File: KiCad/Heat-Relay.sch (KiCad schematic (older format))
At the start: 6 parts, among them K1 G5LE-1A-E_DC12, Q2 MJE340

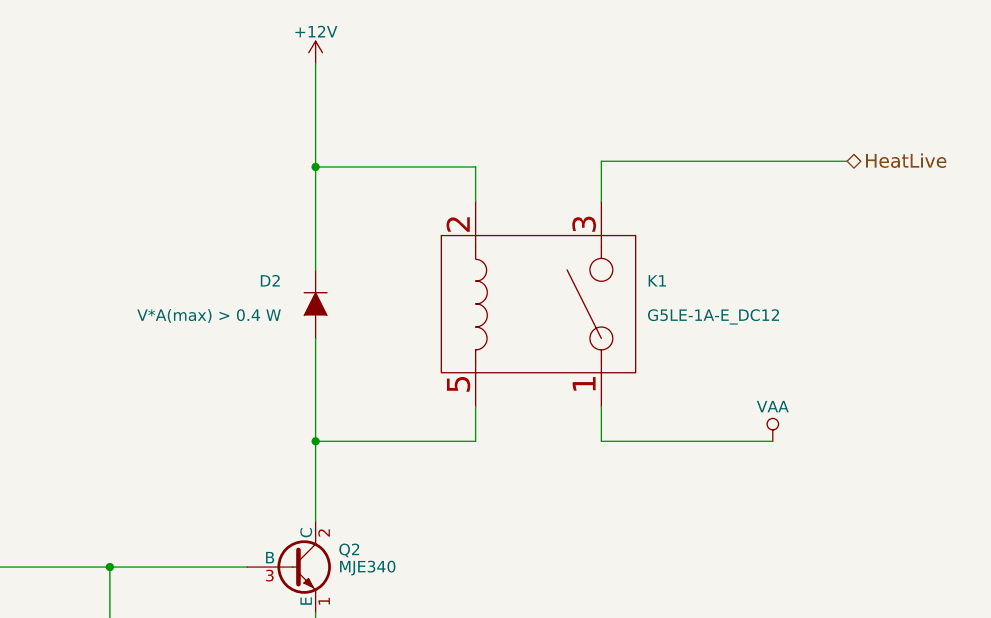
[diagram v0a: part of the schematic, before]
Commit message: power supply placed and routed
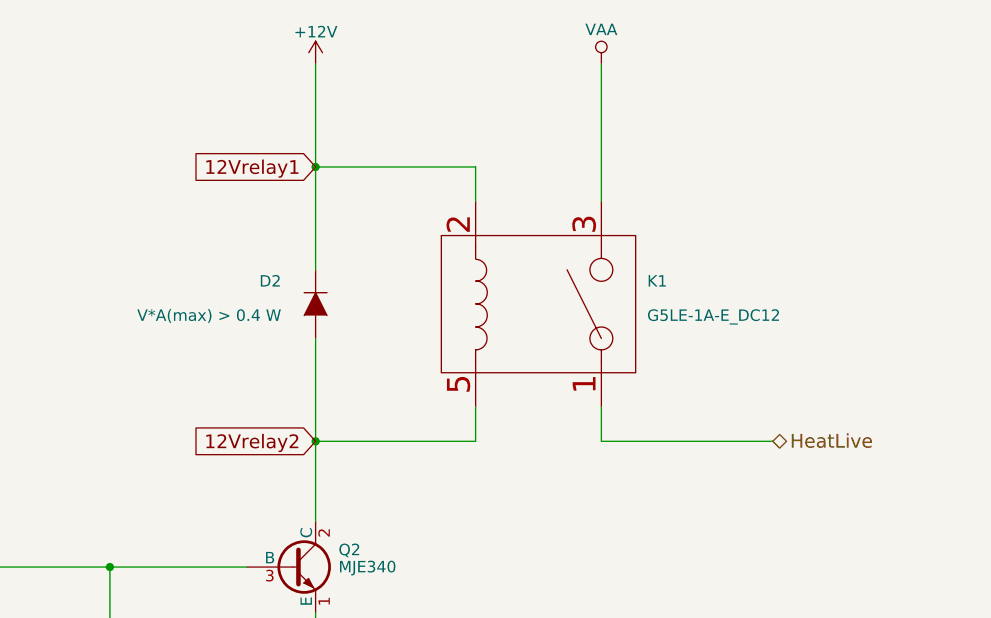
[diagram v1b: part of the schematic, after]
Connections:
- net HeatLive: now also K1.1 (contact_1); no longer K1.3 (contact_2)
- net VAA: now also K1.3 (contact_2); no longer K1.1 (contact_1)
- net 12Vrelay2: now reaches D2.2 (A), K1.5 (coil_2), Q2.2 (C)
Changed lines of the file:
@@
 	0    1    1    0
 $EndComp
-Text HLabel 8725 2625 2    60   BiDi ~ 0
+Text HLabel 8400 3850 2    60   BiDi ~ 0
 HeatLive
 $Comp
 L VAA #PWR024
 U 1 1 56800D0A
-P 8400 3850
-F 0 "#PWR024" H 8400 3700 50  0001 C CNN
-F 1 "VAA" H 8400 4000 50  0000 C CNN
-F 2 "" H 8400 3850 50  0000 C CNN
-F 3 "" H 8400 3850 50  0000 C CNN
-	1    8400 3850
+P 7650 2200
+F 0 "#PWR024" H 7650 2050 50  0001 C CNN
+F 1 "VAA" H 7650 2350 50  0000 C CNN
+F 2 "" H 7650 2200 50  0000 C CNN
+F 3 "" H 7650 2200 50  0000 C CNN
+	1    7650 2200
 	1    0    0    -1
 $EndComp
@@
 	6400 4600 6400 5400
 Wire Wire Line
-	8725 2625 7650 2625
-Wire Wire Line
-	7650 2625 7650 2800
+	7650 2200 7650 2800
 Wire Wire Line
 	7650 3700 7650 3850
 Wire Wire Line
 	7650 3850 8400 3850
+Text GLabel 6400 2650 0    60   Input ~ 0
+12Vrelay1
+Text GLabel 6400 3850 0    60   Input ~ 0
+12Vrelay2
 $EndSCHEMATC

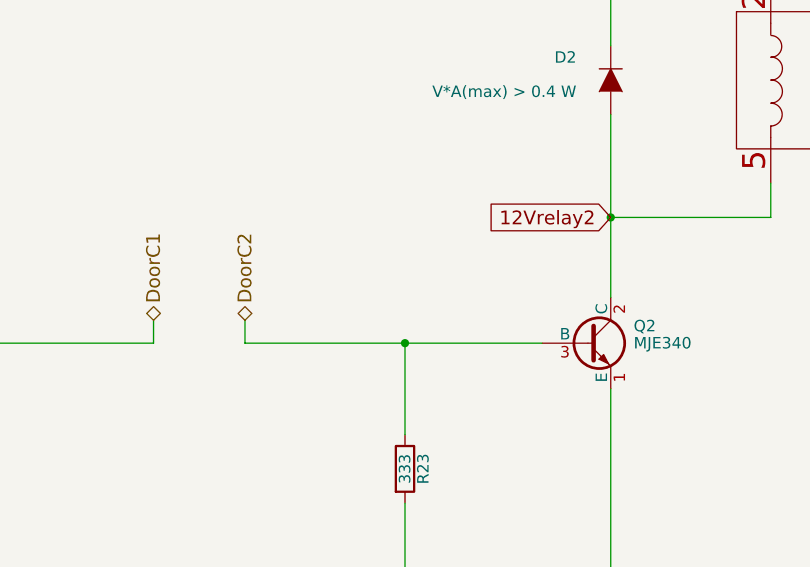
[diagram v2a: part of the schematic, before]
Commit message: connector to front PCB routed
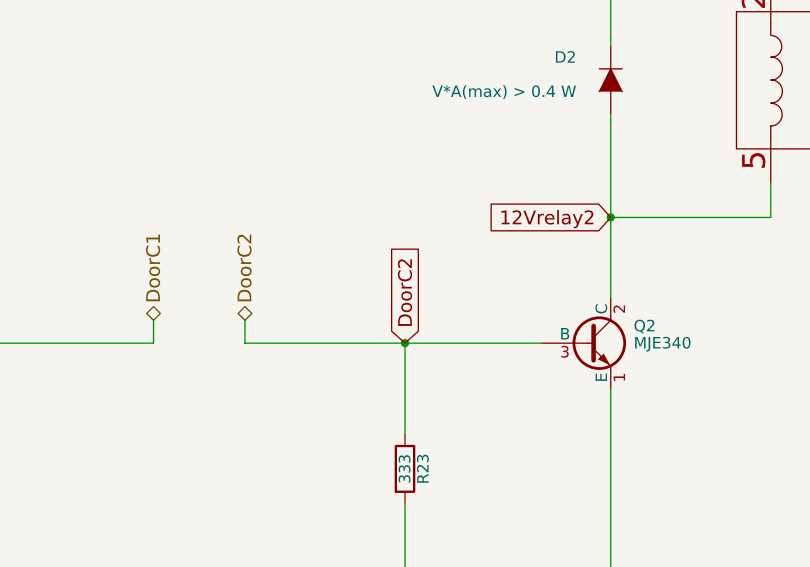
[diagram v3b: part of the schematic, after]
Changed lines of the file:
@@
 Text GLabel 6400 3850 0    60   Input ~ 0
 12Vrelay2
+Text GLabel 5500 4400 1    60   Input ~ 0
+DoorC2
 $EndSCHEMATC
